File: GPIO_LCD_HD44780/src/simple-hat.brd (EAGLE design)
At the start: 87.3 x 61 mm, 36 parts, among them SW1 USER4

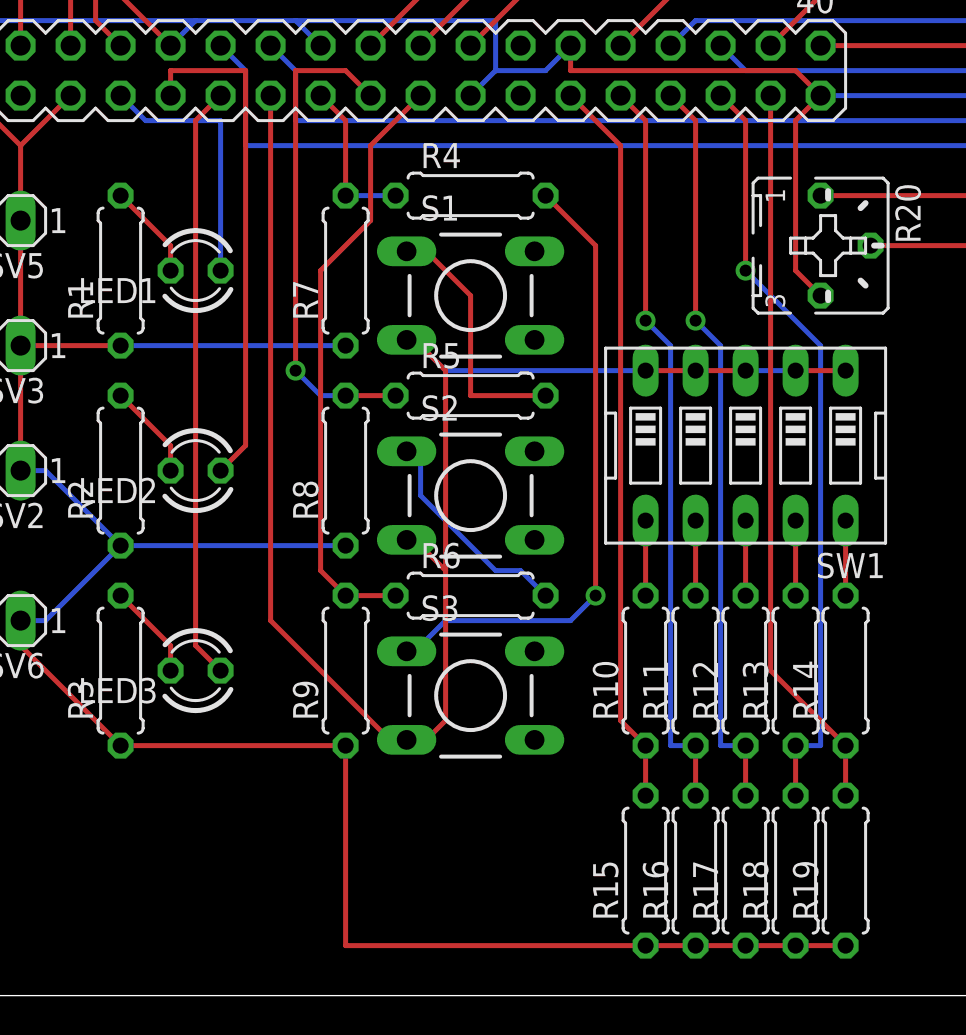
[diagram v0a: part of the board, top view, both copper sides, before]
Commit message: Modified GPIO_LCD circuit.
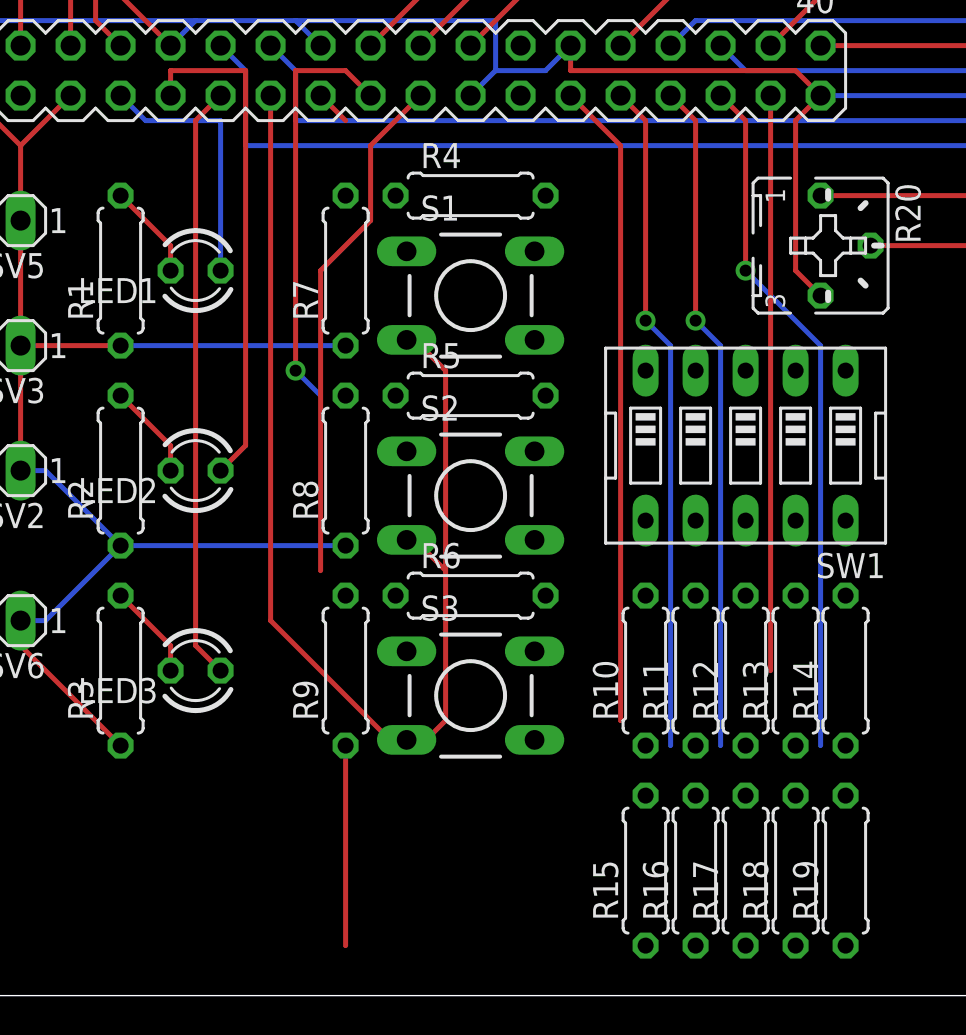
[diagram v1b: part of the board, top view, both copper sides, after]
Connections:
- removed net N$13: R11.2, SW1.7
- removed net N$14: R12.2, SW1.8
- removed net N$15: R10.2, SW1.6
- removed net N$18: R13.2, SW1.9
- removed net N$19: R14.2, SW1.10
- new net N$11: R14.2, R19.2, SW1.10
- new net N$4: R4.1, R7.2, S3.1
- new net N$5: R5.1, R8.2, S1.1
- new net N$6: R6.1, R9.2, S2.1
- new net N$7: R10.2, R15.2, SW1.6
- net GPIO10: no longer R4.1, R7.2
- net GPIO11: no longer R6.1, R9.2
- net GPIO13: no longer R17.2
- net GPIO19: no longer R18.2
- net GPIO26: no longer R19.2
- net GPIO5: no longer R15.2
- net GPIO6: no longer R16.2
- net GPIO9: no longer R5.1, R8.2
- net N$10: now also R13.2, R18.2, SW1.9; no longer R6.2, S2.1
- net N$8: now also R11.2, R16.2, SW1.7; no longer R4.2, S3.1
- net N$9: now also R12.2, R17.2, SW1.8; no longer R5.2, S1.1
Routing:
- net GND: track 229.9 -> 193.1 mm
- net N$8: track 32.1 -> 0.00 mm, vias 1 -> 0
- net +3.3V_17: track 84.6 -> 64.3 mm
- net N$9: track 13.2 -> 0.00 mm
- net N$10: track 11.8 -> 0.00 mm
- net GPIO26: track 37.1 -> 29.2 mm
- net GPIO10: track 8.15 -> 1.80 mm
- net GPIO11: track 30.6 -> 26.2 mm
- net GPIO5: track 37.1 -> 32.8 mm
- net N$19: track 3.81 -> 0.00 mm
- net N$18: track 3.81 -> 0.00 mm
- net N$15: track 3.81 -> 0.00 mm
- net N$14: track 3.81 -> 0.00 mm
- net N$13: track 3.81 -> 0.00 mm
- net GPIO9: track 25.2 -> 21.4 mm
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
